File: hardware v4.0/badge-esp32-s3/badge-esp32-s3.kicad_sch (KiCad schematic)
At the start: 9 parts, among them U1 ESP32-S3-MINI-1-N4R2

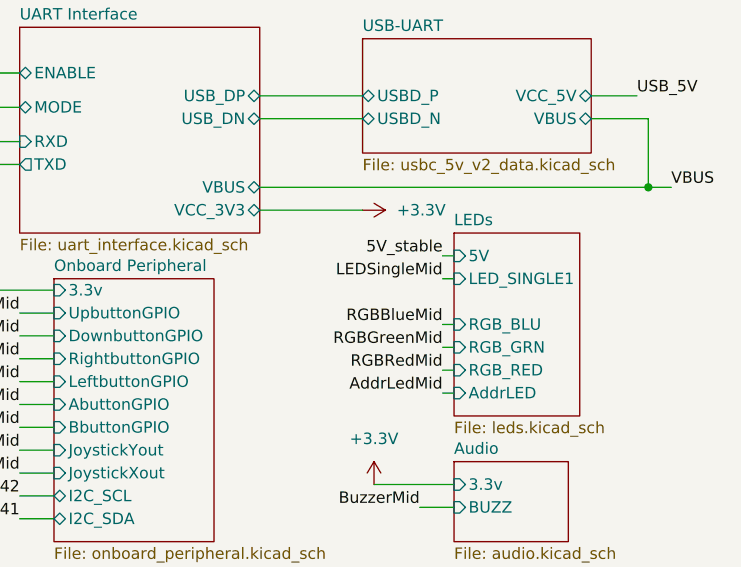
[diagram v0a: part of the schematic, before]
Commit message: started changes for 4.0.1
fixed footprint, joystick collision, Changed to Forced PWM mode for boost converter, Fixed some silkscreen errors
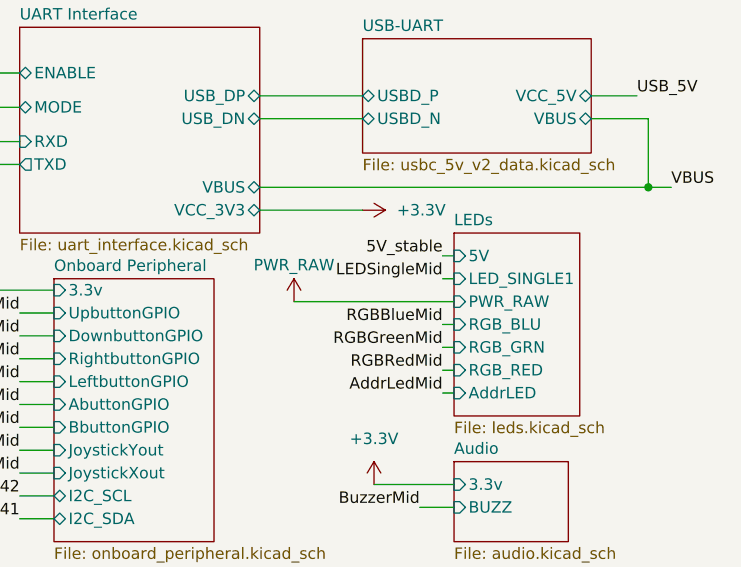
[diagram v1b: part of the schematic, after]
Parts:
- H1, H2, H3, H4: footprint MountingHole_3.2mm_M3_ISO7380_Pad_TopBottom -> MountingHole:MountingHole_3.2mm_M3_ISO7380_Pad_TopBottom
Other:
- sheet LEDs ports: added PWR_RAW; removed none
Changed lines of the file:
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@@
 	(wire
 		(pts
+			(xy 237.49 69.85) (xy 255.27 69.85)
+		)
+		(stroke
+			(width 0)
+			(type default)
+		)
+	)
+	(wire
+		(pts
 			(xy 54.61 71.12) (xy 54.61 72.39)
 		)
@@
 			)
 		)
-		(property "Footprint" "MountingHole_3.2mm_M3_ISO7380_Pad_TopBottom"
+		(property "Footprint" "MountingHole:MountingHole_3.2mm_M3_ISO7380_Pad_TopBottom"
 			(at 20.32 19.05 0)
 			(effects
@@
 	)
 	(symbol
+		(lib_id "power:+4V")
+		(at 237.49 69.85 0)
+		(unit 1)
+		(exclude_from_sim no)
+		(in_bom yes)
+		(on_board yes)
+		(dnp no)
+		(property "Reference" "#PWR087"
+			(at 237.49 73.66 0)
+			(effects
+				(font
+					(size 1.27 1.27)
+				)
+				(hide yes)
+			)
+		)
+		(property "Value" "PWR_RAW"
+			(at 237.49 65.786 0)
+			(effects
+				(font
+					(size 1.27 1.27)
+				)
+			)
+		)
+		(property "Footprint" ""
+			(at 237.49 69.85 0)
+			(effects
+				(font
+					(size 1.27 1.27)
+				)
+				(hide yes)
+			)
+		)
+		(property "Datasheet" ""
+			(at 237.49 69.85 0)
+			(effects
+				(font
+					(size 1.27 1.27)
+				)
+				(hide yes)
+			)
+		)
+		(property "Description" "Power symbol creates a global label with name \"+4V\""
+			(at 237.49 69.85 0)
+			(effects
+				(font
+					(size 1.27 1.27)
+				)
+				(hide yes)
+			)
+		)
+		(pin "1"
+		)
+		(instances
+			(project "badge-esp32-s3"
+				(path "/e2af9a6c-dbe9-4de2-9ba6-ea213a7300ec"
+					(reference "#PWR087")
+					(unit 1)
+				)
+			)
+		)
+	)
+	(symbol
 		(lib_id "power:+3.3V")
 		(at 245.11 59.69 270)
@@
 			)
 		)
-		(property "Footprint" "MountingHole_3.2mm_M3_ISO7380_Pad_TopBottom"
+		(property "Footprint" "MountingHole:MountingHole_3.2mm_M3_ISO7380_Pad_TopBottom"
 			(at 20.32 29.21 0)
 			(effects
@@
 			)
 		)
-		(property "Footprint" "MountingHole_3.2mm_M3_ISO7380_Pad_TopBottom"
+		(property "Footprint" "MountingHole:MountingHole_3.2mm_M3_ISO7380_Pad_TopBottom"
 			(at 20.32 34.29 0)
 			(effects
@@
 			)
 		)
-		(property "Footprint" "MountingHole_3.2mm_M3_ISO7380_Pad_TopBottom"
+		(property "Footprint" "MountingHole:MountingHole_3.2mm_M3_ISO7380_Pad_TopBottom"
 			(at 20.32 24.13 0)
 			(effects
@@
 			(effects
 				(font
+					(size 1.27 1.27)
+				)
+				(justify left)
+			)
+		)
+		(pin "PWR_RAW" input
+			(at 255.27 69.85 180)
+			(effects
+				(font
